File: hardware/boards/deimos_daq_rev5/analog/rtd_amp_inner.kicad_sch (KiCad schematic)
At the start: 18 parts, among them IC4001 INA826AIDR, IC4002 TLV333IDBVR, IC4003 TLV333IDBVR, U4001 NTJD4001NT1G

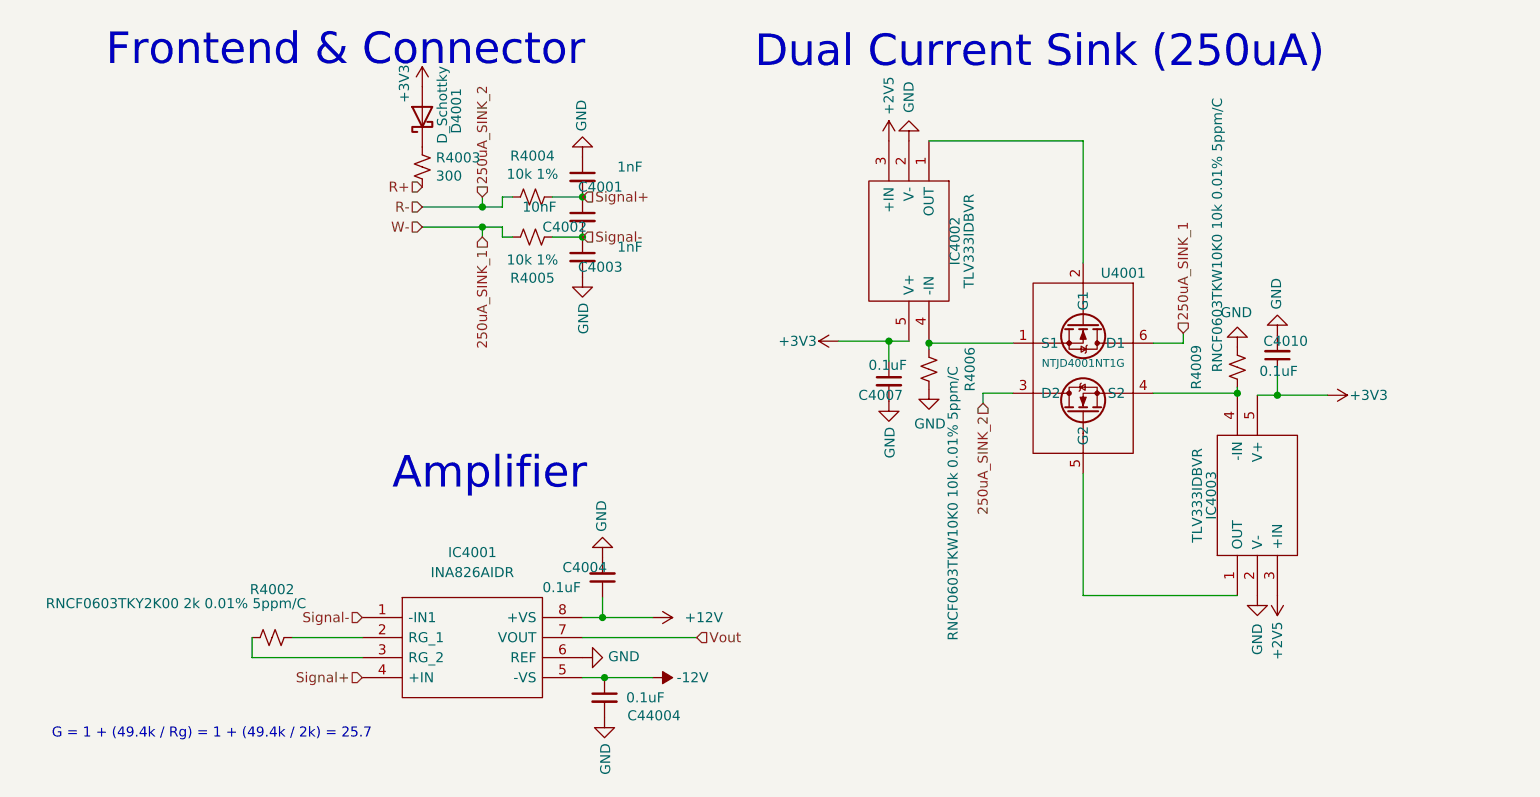
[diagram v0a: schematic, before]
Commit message: add stabilizing integrator to current sinks
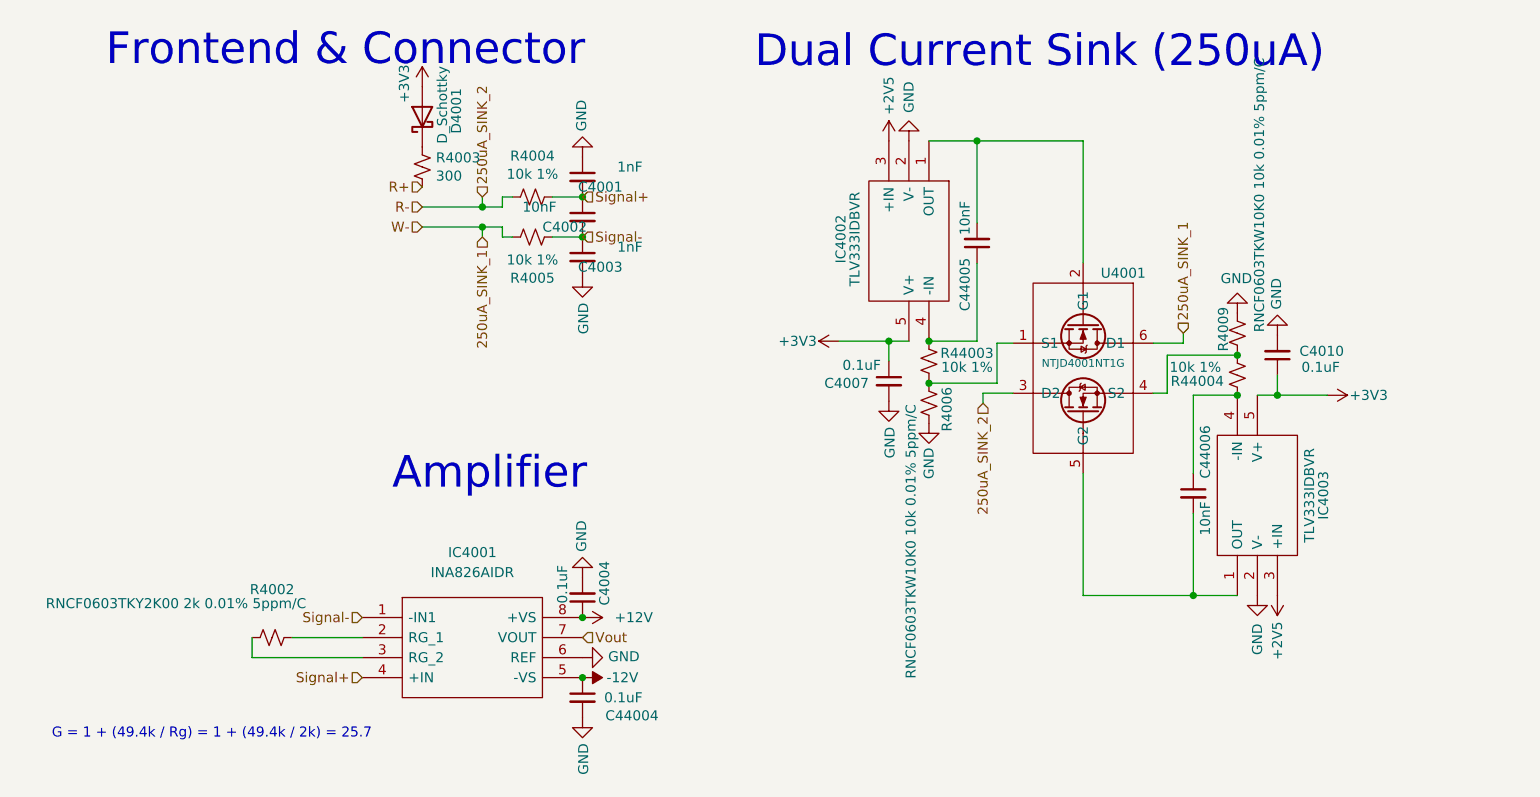
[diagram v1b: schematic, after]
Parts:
- added C44005, C44006: 10nF, Capacitor_SMD:C_0402_1005Metric, symbol Device:C_Small
- added R44003, R44004: 10k 1%, Capacitor_SMD:C_0402_1005Metric, symbol Device:R_Small_US
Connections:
- net at R4009.1, U4001.4 (S2): now also R44004.2; no longer IC4003.4 (-IN)
- net at IC4002.1 (OUT), U4001.2 (G1): now also C44005.2
- net at R4006.1, U4001.1 (S1): now also R44003.1; no longer IC4002.4 (-IN)
- net at IC4003.1 (OUT), U4001.5 (G2): now also C44006.2
- new net: C44005.1, IC4002.4 (-IN), R44003.2
- new net: C44006.1, IC4003.4 (-IN), R44004.1
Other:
- moved on the sheet: C4004, C44004, R4006, R4009

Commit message: restore rev5 and make this rev rev6
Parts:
- removed C44004: 0.1uF, Capacitor_SMD:C_0402_1005Metric, symbol Device:C_Small
- removed C44005, C44006: 10nF, Capacitor_SMD:C_0402_1005Metric, symbol Device:C_Small
- removed R44003, R44004: 10k 1%, Capacitor_SMD:C_0402_1005Metric, symbol Device:R_Small_US
- added D4002: BZT52C3V3, Diode_SMD:D_SOD-323, symbol Device:D_Zener
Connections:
- net -12V is gone; now on net GND: IC4001.5 (-VS)
- net GND: now also D4002.2 (A)
- net Vout: now also D4002.1 (K)
- net at R4009.1, U4001.4 (S2): now also IC4003.4 (-IN)
- net at IC4002.4 (-IN): now also R4006.1, U4001.1 (S1)
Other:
- moved on the sheet: C4004, R4006, R4009

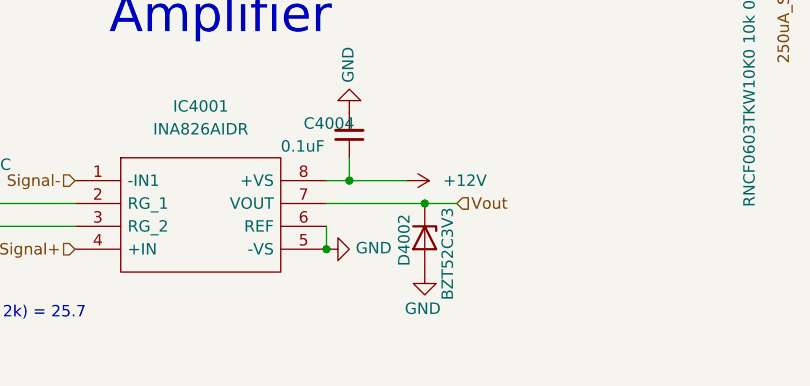
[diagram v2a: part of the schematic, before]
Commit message: put +/12V on all inamps. add 3.3V zener behind first resistor of each filter.
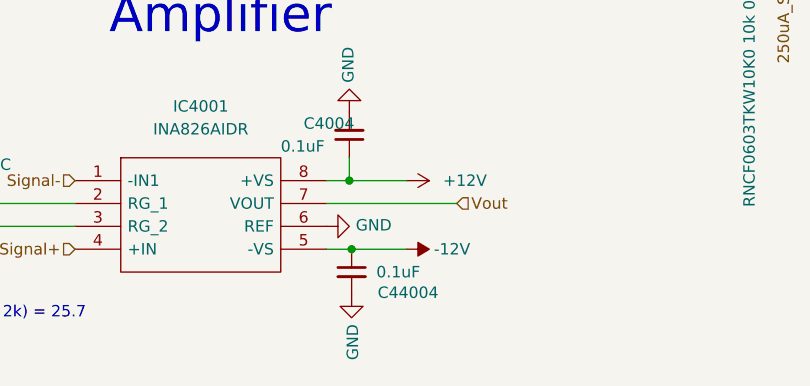
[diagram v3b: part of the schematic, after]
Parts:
- removed D4002: BZT52C3V3, Diode_SMD:D_SOD-323, symbol Device:D_Zener
- added C44004: 0.1uF, Capacitor_SMD:C_0402_1005Metric, symbol Device:C_Small
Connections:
- net GND: now also C44004.2; no longer IC4001.5 (-VS)
- new net -12V: C44004.1, IC4001.5 (-VS)
